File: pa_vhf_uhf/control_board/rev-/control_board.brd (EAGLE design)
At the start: 160 x 100 mm, 0 parts

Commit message: minor updates to control board.
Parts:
- added ADC1: ADS1115, vtgs:MSOP10
- added J1: USB_B_PTH, SparkFun-Connectors:USB-B-PTH
- added U$1: SPX3819M5_5V, kj4qlp:SOT23-5
- added U$2: ATMEGA32U4-AU, adafruit:TQFP44
- added U$3: DECOTEC_102040-002B, vtgs:DECOTEC_102040-002B
- added X1: (no value), SparkFun-Retired:M25D
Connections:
- new net GND: J1.GND
- new net VBUS: J1.VBUS
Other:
- board size 160 x 100 mm -> 69.8 x 69.8 mm

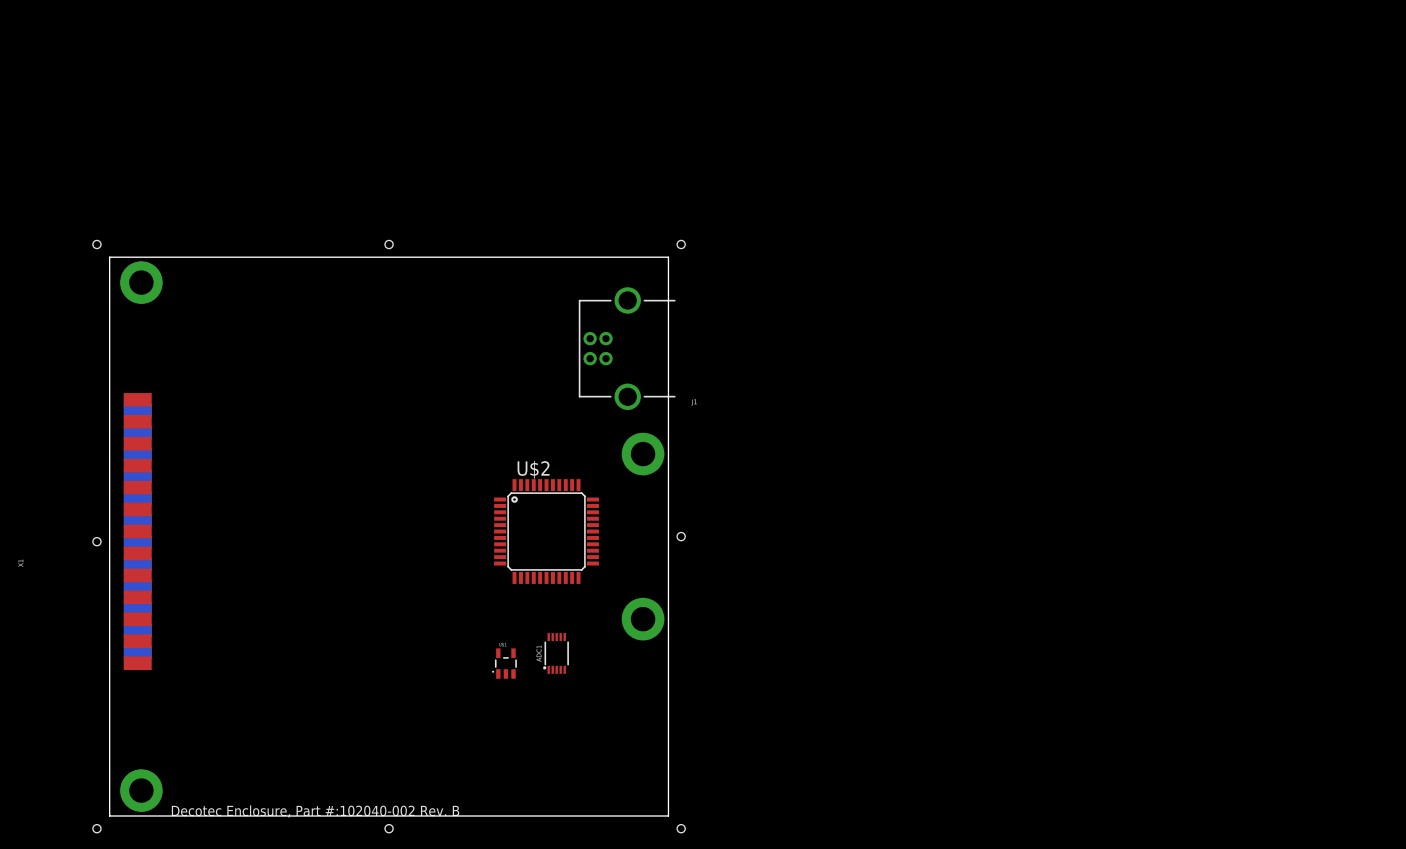
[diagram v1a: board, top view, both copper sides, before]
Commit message: lots of updates, almost done, a bit more tweaking/refining of the layout.  need to double check optocoupler current levels/resistors.
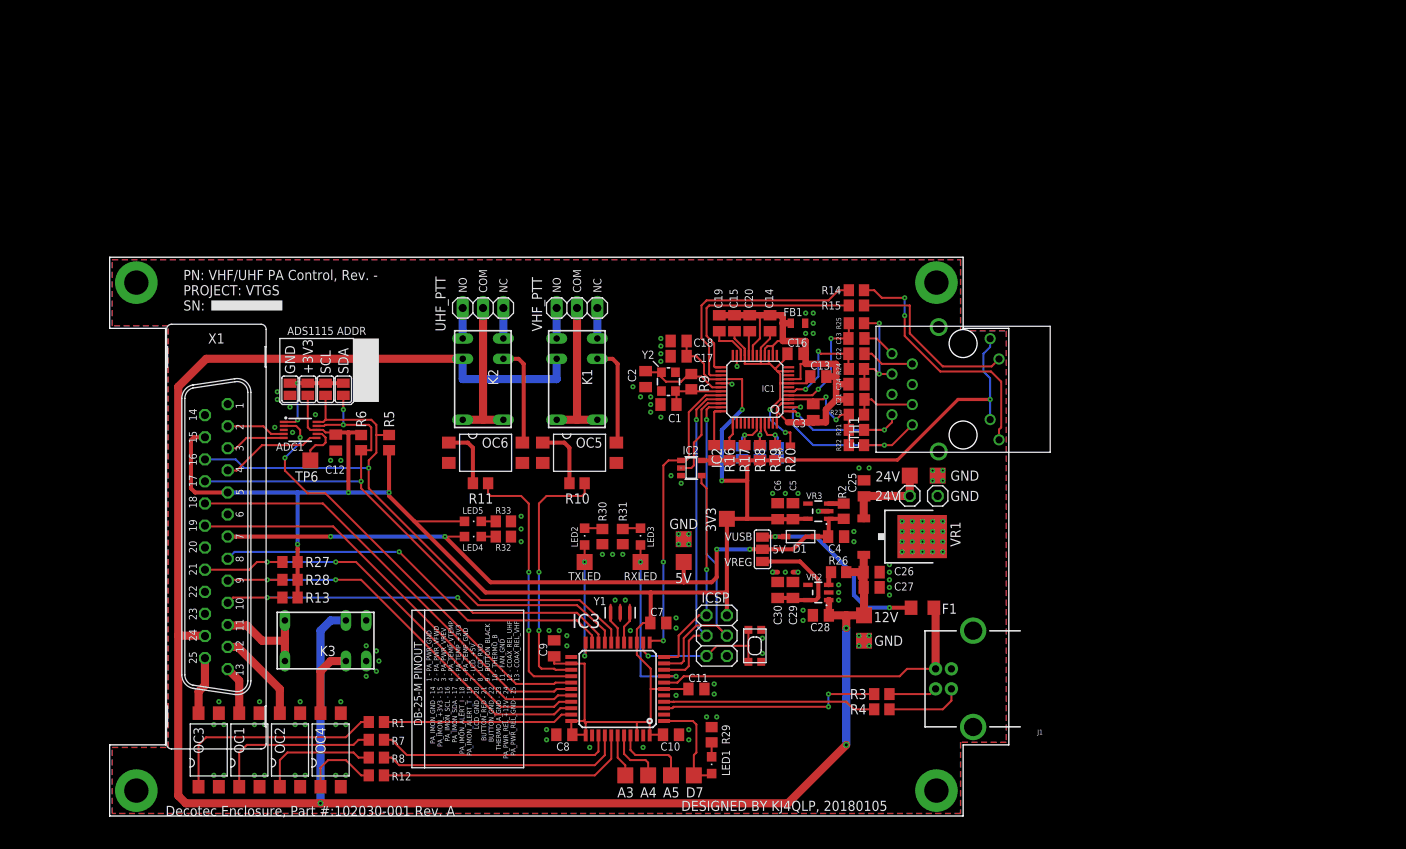
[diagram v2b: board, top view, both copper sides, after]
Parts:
- removed U$1: SPX3819M5_5V, kj4qlp:SOT23-5
- removed U$2: ATMEGA32U4-AU, adafruit:TQFP44
- added 12V, 24V, 3V3, 5V, A3, A4, A5, D7, RXLED, TP1, TP2, TP3, TP6, TXLED: TPSQTP20SQ, testpad:TP20SQ
- added C1, C2: 22pF, rcl:C0805K
- added C10, C12, C27, C30, C6, C7, C8, C9: 1uF, rcl:C0805K
- added C11, C16, C17, C20, C25, C26, C28, C29, C4, C5: 10uF, rcl:C0805K
- added C13, C14, C15, C19, C3: .1uF, rcl:C0805K
- added C18: 0.1uF, rcl:C0805K
- added C21, C24: 0.01uF, rcl:C0805K
- added C22, C23: 6.8nF, rcl:C0805K
- added D1: MBR120, adafruit:SOD-123
- added ETH1: RB1-125BAG1A, vtgs:RB1-125BAG1A
- added F1: 500mA, adafruit:R1206
- added FB1, FB2: (no value), vtgs:0805
- added GND, VIN: (no value), pinhead:1X01
- added IC1: W5500, vtgs:LQFP48
- added IC2: 74AHC1G125DBV, 74xx-little-us:SOT23-5
- added IC3: ATMEGA32U4-AU, adafruit:TQFP44
- added ICSP: (no value), pinhead:2X03
- added K1, K2, K3: G5V1, relay:G5V1
- added LED1, LED2, LED3, LED4, LED5: (no value), adafruit:CHIPLED_0805
- added OC1, OC2, OC3, OC4, OC5, OC6: FOD852, vtgs:SMD4-7
- added R1, R10, R11, R12, R7, R8: 220, rcl:R0805
- added R13, R16, R17, R18, R19, R20, R27, R28, R5, R6: 10k, rcl:R0805
- added R14, R15: 330, rcl:R0805
- added R2, R26: 100k, rcl:R0805
- added R21, R22, R24, R25: 49.9, rcl:R0805
- added R23: 10, rcl:R0805
- added R29, R30, R31, R32, R33: 1k, rcl:R0805
- added R3, R4: 22, rcl:R0805
- added R9: 1M, rcl:R0805
- added SJ1, SJ2, SJ3, SJ4, SJ5, SJ6, SJ7: (no value), jumper:SJ
- added SJ8: (no value), jumper:SJ_2
- added SW1: SPST_TACT-KMR2, adafruit:KMR2
- added UHF_PTT, VHF_PTT: (no value), pinhead:1X03
- added VR1: 7812DT, adafruit:TO252
- added VR2: SPX3819M5_5V, kj4qlp:SOT23-5
- added VR3: SPX3819M5_3V3, kj4qlp:SOT23-5
- added Y1: 8MHz, SparkFun-Clocks:RESONATOR-SMD-3.2X1.3
- added Y2: 25MHz, SparkFun-Clocks:CRYSTAL-SMD-3.2X2.5MM
- U$3: value DECOTEC_102040-002B -> DECOTEC_102030-001AV3; device vtgs:DECOTEC_102040-002B -> vtgs:DECOTEC_102030-001A_V3
- X1: device SparkFun-Retired:M25D -> SparkFun-Retired:M25VB
- moved J1 59.7 mm to (109.2, 17.1)
- moved ADC1 42.5 mm to (23.8, 48.3), turned to 270 degrees
- moved X1 15.9 mm to (13.3, 34.9)
- moved U$3 6.99 mm to (-6.99, 0.00)
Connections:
- new net +12V: 12V.TP, C26.1, C27.1, C28.1, K1.2, K2.2, K3.2, R26.1, VR1.2, VR2.1, X1.24
- new net +24V: 24V.TP, C25.1, VIN.1, VR1.1
- new net +3V3: 3V3.TP, ADC1.8, C10.1, C11.1, C12.1, C17.1, C18.1, C5.1, C6.1, C7.1, C8.1, C9.1, ETH1.11, ETH1.9, FB2.1, IC1.28, IC2.5, IC3.14, IC3.24, IC3.33, IC3.34, IC3.42, IC3.44, IC3.6, ICSP.2, LED5.A, R13.2, R16.2, R17.2, R18.2, R19.2, R20.2, R27.2, R28.2, R5.2, R6.2, SJ3.2, VR3.5, X1.15, X1.5
- new net +5V: 5V.TP, C4.1, D1.C, LED4.A, R2.1, SJ8.2, VR3.1, X1.7
- new net 0_RX_THERMO: IC3.20, R13.1, X1.10
- new net 10_BUTTON_RED: IC3.30, R27.1, X1.21
- new net 11_CS: IC1.32, IC2.1, IC3.12
- new net 12_UHF_PTT_REL: IC3.26, R11.1
- new net 13_PA_PWR_REL: IC3.32, R1.1
- new net 14_MISO_MCU: IC2.4, IC3.11, ICSP.1
- new net 15_SCK: IC1.33, IC3.9, ICSP.3
- new net 16_MOSI: IC1.35, IC3.10, ICSP.4
- new net 1_TX: IC3.21, X1.8
- new net 4_VHF_PTT_REL: IC3.25, R10.1
- new net 5_BUTTON_BLACK: IC3.31, R28.1, X1.9
- new net 6_ALERT_ADC: ADC1.2, IC3.27
- new net 8_ALERT_I: IC3.28, X1.18
- new net 9_ALERT_T: IC3.29, X1.19
- new net A0_VHF_COAX_REL: IC3.36, R7.1
- new net A1_UHF_COAX_REL: IC3.37, R8.1
- new net A2_PA_FAN: IC3.38, R12.1
- new net A3: A3.TP, IC3.39
- new net A4: A4.TP, IC3.40
- new net A5: A5.TP, IC3.41
- new net ACTLED: ETH1.10, R14.1
- new net ADDR: ADC1.1, SJ1.1, SJ2.1, SJ3.1, SJ4.1
- new net AGND: C13.2, C14.2, C15.2, C16.2, C19.2, C20.2, C21.2, C24.2, C3.2, FB1.2, IC1.14, IC1.16, IC1.19, IC1.3, IC1.48, IC1.9
- new net D7: D7.TP, IC3.1, LED1.A
- new net FAN: K3.5, K3.6, X1.11
- new net IRQ: IC1.36, R16.1
- new net LINKLED: ETH1.12, R15.1
- new net MISO: IC1.34, IC2.2
- new net N$1: OC3.1, R1.2
- new net N$10: IC3.4, R4.2
- new net N$11: J1.D+, R4.1
- new net N$12: OC1.1, R7.2
- new net N$13: OC2.1, R8.2
- new net N$14: IC1.37, R17.1
- new net N$15: OC5.1, R10.2
- new net N$16: LED1.C, R29.2
- new net N$17: LED2.C, R30.2
- new net N$18: LED4.C, R32.2
- new net N$19: LED5.C, R33.2
- new net N$2: K3.9, OC4.4
- new net N$20: OC6.1, R11.2
- new net N$21: OC4.1, R12.2
- new net N$22: K1.9, OC5.4
- new net N$23: K2.9, OC6.4
- new net N$24: LED3.C, R31.2
- new net N$29: IC1.27, R14.2
- new net N$3: R2.2, VR3.3
- new net N$30: IC1.25, R15.2
- new net N$31: C29.1, C30.1, SJ8.3, VR2.5
- new net N$33: C20.1, IC1.20
- new net N$34: C19.1, IC1.22
- new net N$35: C23.1, ETH1.8
- new net N$36: C22.1, ETH1.7
- new net N$37: C24.1, ETH1.6, R24.1, R25.1
- new net N$38: R26.2, VR2.3
- new net N$39: D1.A, F1.2, SJ8.1
- new net N$4: IC3.17, Y1.1
- new net N$5: IC3.16, Y1.3
- new net N$6: C1.1, IC1.31, R9.1, Y2.1
- new net N$7: C2.1, IC1.30, R9.2, Y2.3
- new net N$8: J1.D-, R3.1
- new net N$9: IC3.3, R3.2
- new net PA_PWR_REL: OC3.4, X1.25
- new net PMODE0: IC1.45, R20.1, SJ5.1
- new net PMODE1: IC1.44, R19.1, SJ6.1
- new net PMODE2: IC1.43, R18.1, SJ7.1
- new net RST: IC3.13, ICSP.5, SW1.2, SW1.4
- new net RX+: C22.2, IC1.6, R24.2
- new net RX-: C23.2, IC1.5, R25.2
- new net RXLED: IC3.8, LED3.A, RXLED.TP
- new net SCL: ADC1.10, IC3.18, R5.1, SJ1.2, X1.16
- new net SDA: ADC1.9, IC3.19, R6.1, SJ2.2, X1.17
- new net TCT: C21.1, ETH1.3, R23.1
- new net TX+: ETH1.1, IC1.2, R22.1
- new net TX-: ETH1.2, IC1.1, R21.1
- new net TXLED: IC3.22, LED2.A, TXLED.TP
- new net UHF_COAX_REL: OC2.4, X1.12
- new net UHF_PTT_COM: K2.5, K2.6, UHF_PTT.2
- new net UHF_PTT_NC: K2.10, UHF_PTT.3
- new net UHF_PTT_NO: K2.1, UHF_PTT.1
- new net VDDA: C13.1, C14.1, C15.1, C16.1, C3.1, FB2.2, IC1.11, IC1.15, IC1.17, IC1.21, IC1.4, IC1.8, R21.2, R22.2, R23.2
- new net VHF_COAX_REL: OC1.4, X1.13
- new net VHF_PTT_COM: K1.5, K1.6, VHF_PTT.2
- new net VHF_PTT_NC: K1.1, VHF_PTT.1
- new net VHF_PTT_NO: K1.10, VHF_PTT.3
- new net V_3: ADC1.7, TP6.TP
- new net V_FWD: ADC1.4, X1.2
- new net V_REV: ADC1.5, X1.3
- new net V_TEMP: ADC1.6, X1.4
- net GND: now also ADC1.3, C1.2, C10.2, C11.2, C12.2, C17.2, C18.2, C2.2, C25.2, C26.2, C27.2, C28.2, C29.2, C30.2, C4.2, C5.2, C6.2, C7.2, C8.2, C9.2, ETH1.13, ETH1.14, ETH1.4, ETH1.5, FB1.1, GND.1, IC1.23, IC1.29, IC2.3, IC3.15, IC3.23, IC3.35, IC3.43, IC3.5, ICSP.6, J1.SHLD1, J1.SHLD2, K3.10, OC1.2, OC1.3, OC2.2, OC2.3, OC3.2, OC3.3, OC4.2, OC4.3, OC5.2, OC5.3, OC6.2, OC6.3, R29.1, R30.1, R31.1, R32.1, R33.1, SJ4.2, SJ5.2, SJ6.2, SJ7.2, SW1.1, SW1.3, TP1.TP, TP2.TP, TP3.TP, U$3.PAD1, U$3.PAD2, U$3.PAD3, U$3.PAD4, VR1.3, VR2.2, VR3.2, X1.1, X1.14, X1.20, X1.22, X1.23, X1.6, Y1.2
- net VBUS: now also F1.1, IC3.7
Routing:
- net +3V3: track 0.00 -> 287.4 mm, vias 0 -> 6
- net +12V: track 0.00 -> 253.9 mm, vias 0 -> 3
- net +5V: track 0.00 -> 90.9 mm, vias 0 -> 4
- net SCL: track 0.00 -> 80.9 mm, vias 0 -> 1
- net SDA: track 0.00 -> 78.4 mm, vias 0 -> 3
- net AGND: track 0.00 -> 58.7 mm
- net 10_BUTTON_RED: track 0.00 -> 55.8 mm, vias 0 -> 2
- net 8_ALERT_I: track 0.00 -> 55.7 mm
- net 6_ALERT_ADC: track 0.00 -> 55.0 mm, vias 0 -> 2
- net 9_ALERT_T: track 0.00 -> 55.0 mm
- net 5_BUTTON_BLACK: track 0.00 -> 52.2 mm, vias 0 -> 2
- net 0_RX_THERMO: track 0.00 -> 51.5 mm, vias 0 -> 2
- net 1_TX: track 0.00 -> 51.1 mm, vias 0 -> 1
- net VDDA: track 0.00 -> 50.0 mm, vias 0 -> 4
- net 16_MOSI: track 0.00 -> 43.2 mm, vias 0 -> 1
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- added copper zone on layer 1, net GND
- added copper zone on layer 16, net GND
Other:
- board size 69.8 x 69.8 mm -> 112.4 x 69.8 mm
- board text added: "+3V3"
- board text added: "0 0 0 = 10BT Half-duplex, Auto-negotiation disabled 0 0 1 = 10BT Full-duplex, Auto-negotiation disabled 0 1 0 = 100BT Half-duplex, Auto-negotiation disabled 0 1 1 = 100BT Full-duplex, Auto-negotiation disabled 1 0 0 = 100BT Half-duplex, Auto-negotiation enabled 1 1 1 = All capable, Auto-negotiation enabled (DEFAULT)"
- board text added: "1 - PA_PWR_GND 2 - PA_PWR_VFWD 3 - PA_PWR_VREV 4 - PA_TEMP_VTEMP 5 - PA_TEMP_+3V3 6 - PA_TEMP_GND 7 - LCD_+5V 8 - LCD_RXD 9 - BUTTON_BLACK 10 - THERMO_B 11 - FAN_GND 12 - COAX_REL_UHF 13 - COAX_REL_VHF"
- board text added: "24V"
- board text added: "5V"
- board text added: "ADS1115 ADDR"
- board text added: "COM"
- board text added: "DB-25-M PINOUT"
- board text added: "DESIGNED BY KJ4QLP, 20180105"
- board text added: "GND"
- board text added: "IC2"
- board text added: "NC"
- board text added: "NO"
- board text added: "PA_IMON_GND - 14 PA_IMON_+3V3 - 15 PA_IMON_SCL - 16 PA_IMON_SDA - 17 PA_IMON_ALERT_I - 18 PA_IMON_ALERT_T - 19 LCD_GND - 20 BUTTON_RED - 21 BUTTON_GND - 22 THERMO_A_GND - 23 PA_PWR_REL_+12V - 24 PA_PWR_REL_GND - 25"
- board text added: "PM0"
- board text added: "PM1"
- board text added: "PM2"
- board text added: "PN: VHF/UHF PA Control, Rev. -"
- board text added: "PROJECT: VTGS"
- board text added: "SCL"
- board text added: "SDA"
- board text added: "SN:"
- board text added: "VREG"
- board text added: "VUSB"

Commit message: Final Commit for Rev-.  This version submitted to osh park for fab.
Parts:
- removed C30: 1uF, rcl:C0805K
- removed GND, VIN: (no value), pinhead:1X01
- removed TP2, TP3, TP6: TPSQTP20SQ, testpad:TP20SQ
- removed VR1: 7812DT, adafruit:TO252
- added CASE_TEMP: (no value), pinhead:1X03
- added DIS: (no value), pinhead:1X02
- added KA278R12C: (no value), pinhead:1X06
- added R34, R35, R36, R37, R38, R39: 10, rcl:R0805
- added R40: 10k, rcl:R0805
- C1, C2: value 22pF -> 12pF
- C18: value 0.1uF -> .1uF
- C25: value 10uF -> 33uF; device rcl:C0805K -> rcl:PANASONIC_C
- C26: value 10uF -> 100uF; device rcl:C0805K -> rcl:PANASONIC_D
- C27: value 1uF -> 10uF
- C29: value 10uF -> 1uF
- Y2: value 25MHz -> 25MHz, 10pF
- moved LED4 40.7 mm to (86.0, 35.9), turned to 180 degrees
- moved LED5 38.7 mm to (84.1, 35.9), turned to 180 degrees
- moved R32 36.9 mm to (86.0, 32.1), turned to 90 degrees
- moved R33 35.2 mm to (84.1, 32.1), turned to 90 degrees
- moved 24V 33.4 mm to (102.2, 9.21)
- moved C25 29.8 mm to (98.1, 11.4), turned to 270 degrees
- moved 12V 25.1 mm to (81.0, 3.81)
- moved TP1 21.1 mm to (86.7, 41.6)
- moved 5V 20.0 mm to (89.2, 41.6)
- moved C26 19.4 mm to (91.8, 11.4), turned to 270 degrees
- moved 3V3 15.3 mm to (91.8, 41.6)
- moved R26 12.4 mm to (103.5, 31.4), turned to 90 degrees
- moved VR2 12.3 mm to (100.3, 31.4)
- moved C5 12.0 mm to (97.2, 40.3)
- moved C6 12.0 mm to (95.2, 40.3)
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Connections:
- removed net V_3: ADC1.7, TP6.TP
- new net N$25: OC5.3, R34.1
- new net N$26: OC6.3, R35.1
- new net N$27: OC4.3, R36.1
- new net N$28: OC1.3, R37.1
- new net N$32: OC2.3, R38.1
- new net N$40: OC3.3, R39.1
- new net N$41: DIS.1, KA278R12C.5, R40.1
- new net V_CASE: ADC1.7, CASE_TEMP.3
- net +12V: now also C26.+, KA278R12C.3; no longer C26.1, C28.1, VR1.2
- net +24V: now also C25.+, KA278R12C.1, KA278R12C.2, R40.2; no longer C25.1, VIN.1, VR1.1
- net +3V3: now also CASE_TEMP.2
- net GND: now also C25.-, C26.-, CASE_TEMP.1, DIS.2, KA278R12C.4, KA278R12C.6, R34.2, R35.2, R36.2, R37.2, R38.2, R39.2; no longer C25.2, C26.2, C30.2, GND.1, OC1.3, OC2.3, OC3.3, OC4.3, OC5.3, OC6.3, TP2.TP, TP3.TP, VR1.3
- net N$31: now also C28.1; no longer C30.1
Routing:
- net V_CASE: track 0.00 -> 32.3 mm, vias 0 -> 2
- net +12V: track 253.9 -> 280.8 mm, vias 3 -> 4
- net +24V: track 11.0 -> 36.5 mm
- net N$40: track 0.00 -> 23.3 mm
- net +3V3: track 287.4 -> 306.4 mm, vias 6 -> 7
- net N$28: track 0.00 -> 17.9 mm
- net +5V: track 90.9 -> 103.9 mm, vias 4 -> 6
- net N$41: track 0.00 -> 6.35 mm
- net N$31: track 15.5 -> 9.32 mm
- net V_3: track 5.52 -> 0.00 mm
- net RST: track 19.0 -> 24.4 mm
- net N$39: track 25.5 -> 22.2 mm, vias 2 -> 0
- net N$9: track 27.9 -> 31.0 mm
- net N$27: track 0.00 -> 2.70 mm
- net N$25: track 0.00 -> 2.61 mm
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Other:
- board text added: "+12V"
- board text added: "+24V"
- board text added: "3V3"
- board text added: "DESIGNED BY KJ4QLP, 20180108"
- board text added: "DIS"
- board text added: "MISO"
- board text added: "MOSI"
- board text added: "RESET"
- board text added: "RST"
- board text added: "SCK"
- board text added: "V_CASE"
- board text removed: "24V"
- board text removed: "DESIGNED BY KJ4QLP, 20180105"
- board text removed: "IC2"
